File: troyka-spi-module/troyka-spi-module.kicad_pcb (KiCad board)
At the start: 2 copper layers, 25.4 x 25.4 mm, 5 parts, among them J1 UP (A), J2 DOWN (A)

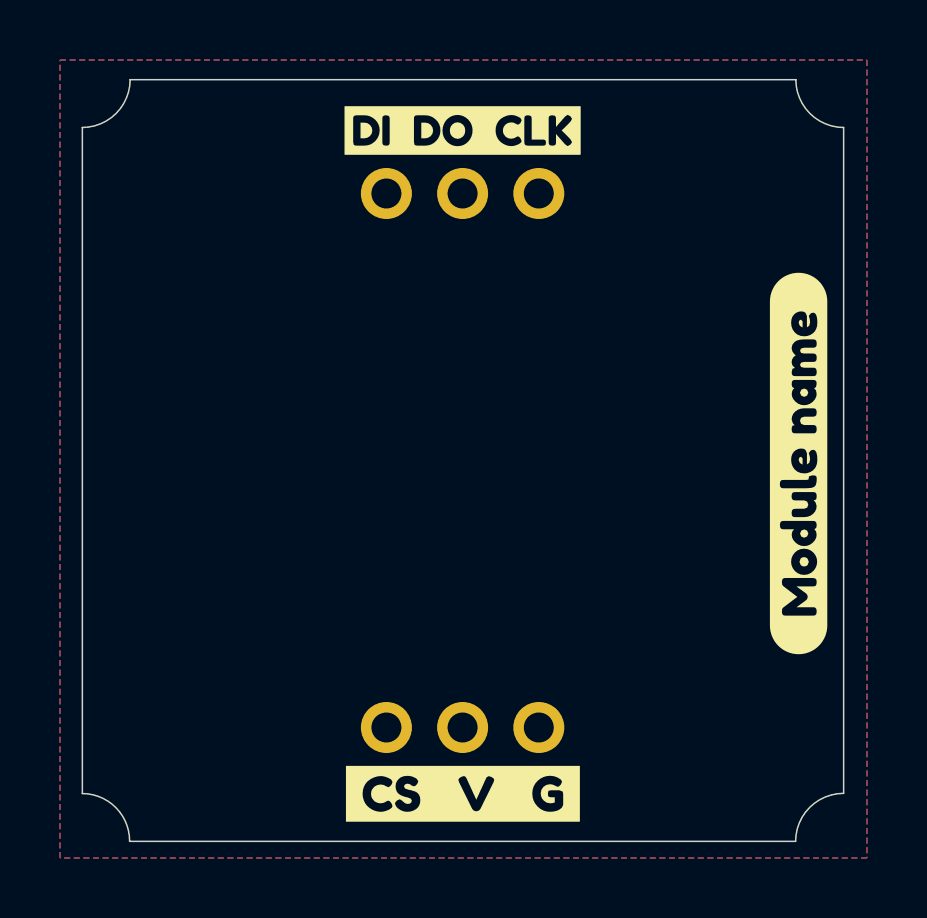
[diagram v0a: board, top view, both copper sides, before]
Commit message: Update templates and CI
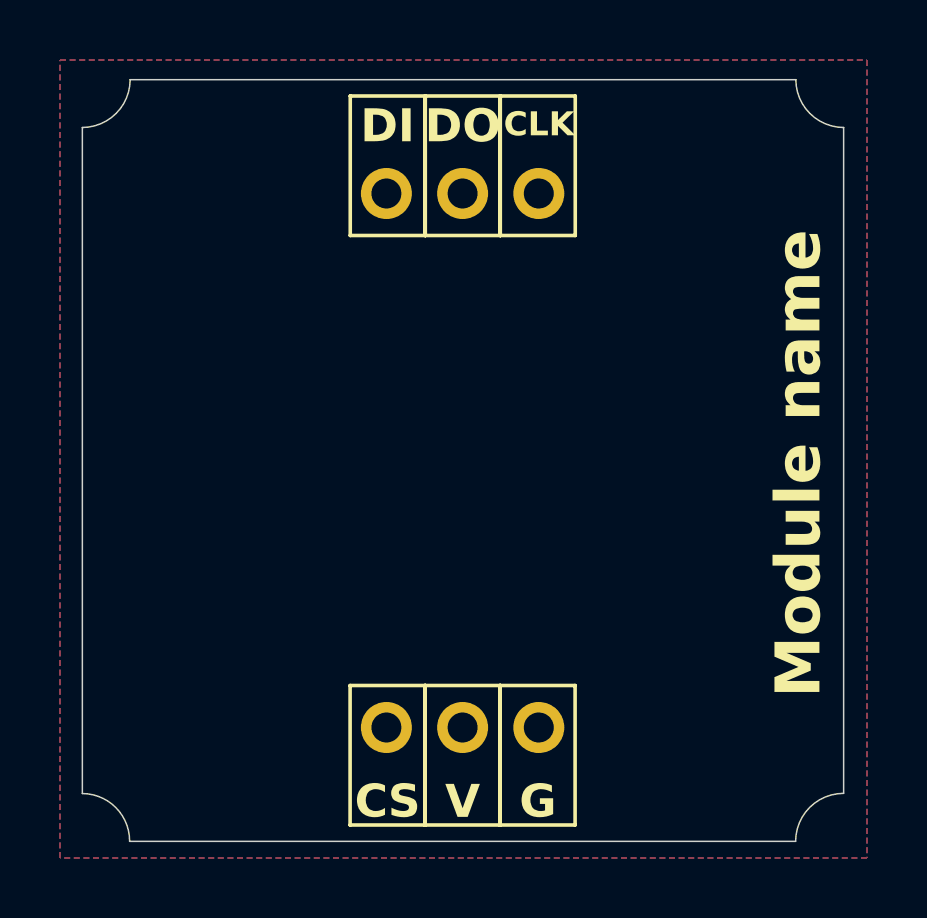
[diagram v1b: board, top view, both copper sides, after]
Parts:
- removed kibuzzard-63E392E0: G***, kibuzzard-63E392E0
- removed kibuzzard-63E39612: G***, kibuzzard-63E39612
- removed kibuzzard-63E39651: G***, kibuzzard-63E39651
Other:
- board text added: "CLK"
- board text added: "CS"
- board text added: "DI"
- board text added: "DO"
- board text added: "G"
- board text added: "Module name"
- board text added: "V"
